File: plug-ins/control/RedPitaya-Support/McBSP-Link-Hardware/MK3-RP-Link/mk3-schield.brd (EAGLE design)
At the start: 59.4 x 51.2 mm, 16 parts, among them U1 SN65MLVD202A, U2 SN65MLVD202A, U3 SN65MLVD202A

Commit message: updated gnd routing
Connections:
- net GND: now also J1.3, J1.4, J1.5, J1.6
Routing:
- net GND: track 112.2 -> 146.7 mm
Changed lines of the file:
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@@
 <wire x1="17.145" y1="9.5758" x2="17.1990625" y2="9.554475" width="0.1524" layer="1"/>
 <wire x1="7.5438" y1="11.0998" x2="7.427" y2="11.237" width="0.1524" layer="1"/>
+<contactref element="J1" pad="3"/>
+<contactref element="J1" pad="4"/>
+<contactref element="J1" pad="5"/>
+<contactref element="J1" pad="6"/>
+<wire x1="51.9684" y1="36.1188" x2="50.9016" y2="36.1188" width="0.254" layer="1"/>
+<wire x1="50.9016" y1="36.1188" x2="49.6824" y2="36.1188" width="0.254" layer="1"/>
+<wire x1="49.6824" y1="36.1188" x2="49.572" y2="36.067" width="0.1524" layer="1"/>
+<wire x1="51.9684" y1="36.1188" x2="52.112" y2="36.067" width="0.1524" layer="1"/>
+<wire x1="53.34" y1="38.7096" x2="50.9016" y2="38.7096" width="0.254" layer="1"/>
+<wire x1="50.9016" y1="38.7096" x2="50.842" y2="38.607" width="0.1524" layer="1"/>
+<wire x1="53.34" y1="38.7096" x2="53.382" y2="38.607" width="0.1524" layer="1"/>
+<wire x1="50.9016" y1="38.5572" x2="50.9016" y2="36.1188" width="0.254" layer="1"/>
+<wire x1="50.9016" y1="38.5572" x2="50.842" y2="38.607" width="0.1524" layer="1"/>
+<wire x1="49.53" y1="25.7048" x2="49.53" y2="35.9664" width="0.254" layer="16"/>
+<wire x1="39.6748" y1="15.5956" x2="49.53" y2="25.7048" width="0.1524" layer="16"/>
+<wire x1="39.6748" y1="14.1224" x2="39.6748" y2="15.5956" width="0.1524" layer="16"/>
+<wire x1="39.624" y1="13.4112" x2="39.6748" y2="14.1224" width="0.1524" layer="16"/>
+<wire x1="49.53" y1="35.9664" x2="49.572" y2="36.067" width="0.1524" layer="16"/>
+<wire x1="39.624" y1="13.4112" x2="39.7002" y2="13.3858" width="0.1524" layer="16"/>
 </signal>
 <signal name="CLKR0">

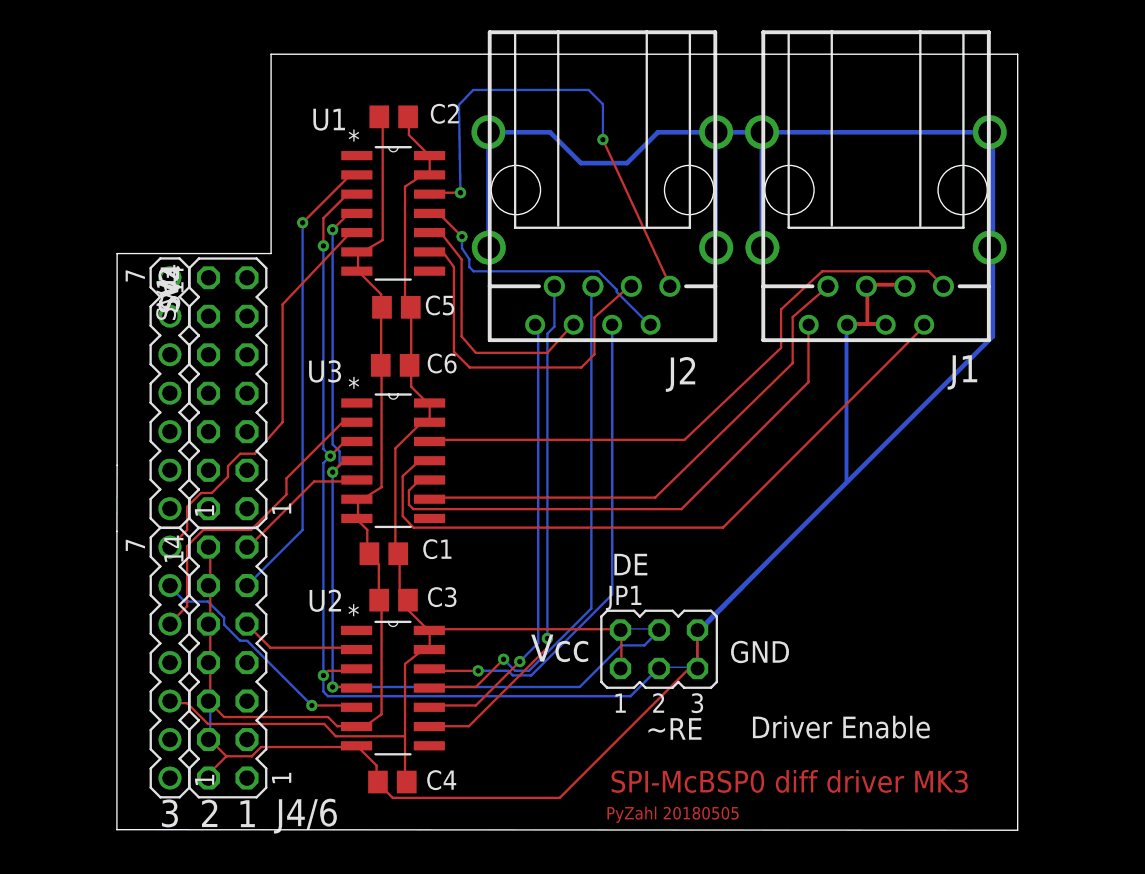
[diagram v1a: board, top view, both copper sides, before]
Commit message: updated MK3 Link Design Files, added detailed BOM (xlsx)
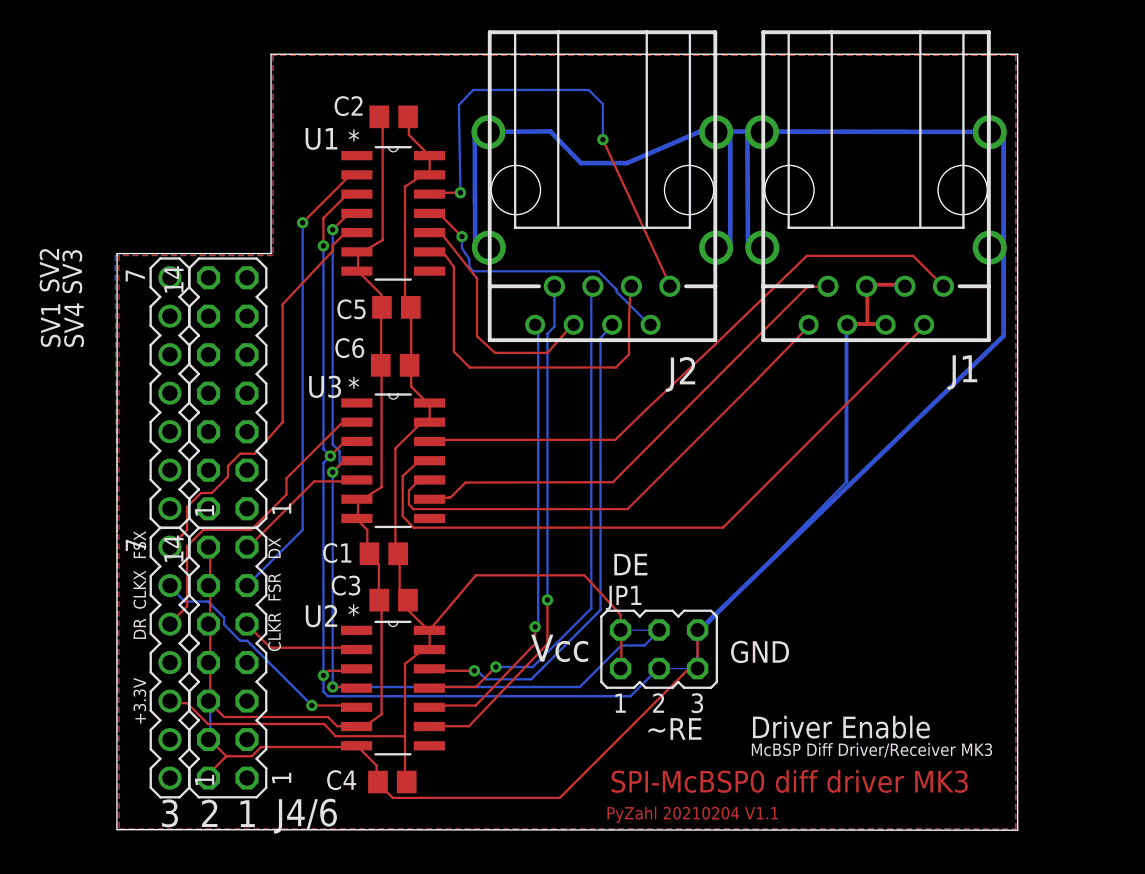
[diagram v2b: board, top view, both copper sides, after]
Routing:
- net GND: track 146.7 -> 252.8 mm
- net N$13: track 75.8 -> 0.00 mm
- net N$15: track 7.73 -> 0.00 mm
- net N$16: track 7.37 -> 0.00 mm
- net N$14: track 7.37 -> 0.00 mm
- net VCC+3.3V: track 81.5 -> 85.3 mm
- net N$4: track 36.4 -> 34.3 mm
- net N$3: track 33.8 -> 32.1 mm
- net VCC: track 0.00 -> 1.27 mm
- net N$18: track 1.27 -> 0.00 mm
- net N$17: track 1.27 -> 0.00 mm
- net N$7: track 23.5 -> 24.7 mm
- net N$8: track 16.8 -> 16.1 mm
- net N$1: track 40.4 -> 39.7 mm
- net N$10: track 34.8 -> 34.2 mm
- added copper zone on layer 1, net GND
- added copper zone on layer 16, net GND
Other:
- board text added: "+3.3V"
- board text added: "CLKR"
- board text added: "CLKX"
- board text added: "DR"
- board text added: "DX"
- board text added: "FSR"
- board text added: "FSX"
- board text added: "McBSP Diff Driver/Receiver MK3"
- board text added: "PyZahl 20210204 V1.1"
- board text removed: "PyZahl 20180505"
